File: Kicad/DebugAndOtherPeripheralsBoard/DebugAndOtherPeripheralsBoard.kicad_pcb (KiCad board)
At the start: 2 copper layers, 234.5 x 198.2 mm, 118 parts, among them J1 SCL, SDA, +, GND, J10 USB RWGBS, J11 Standoff Hole, J12 Standoff Hole, J13 Standoff Hole, J14 Standoff Hole, J15 Standoff Hole, J2 Conn_01x08_Pin, J3 Conn_01x01_Pin, J4 Conn_01x01_Pin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

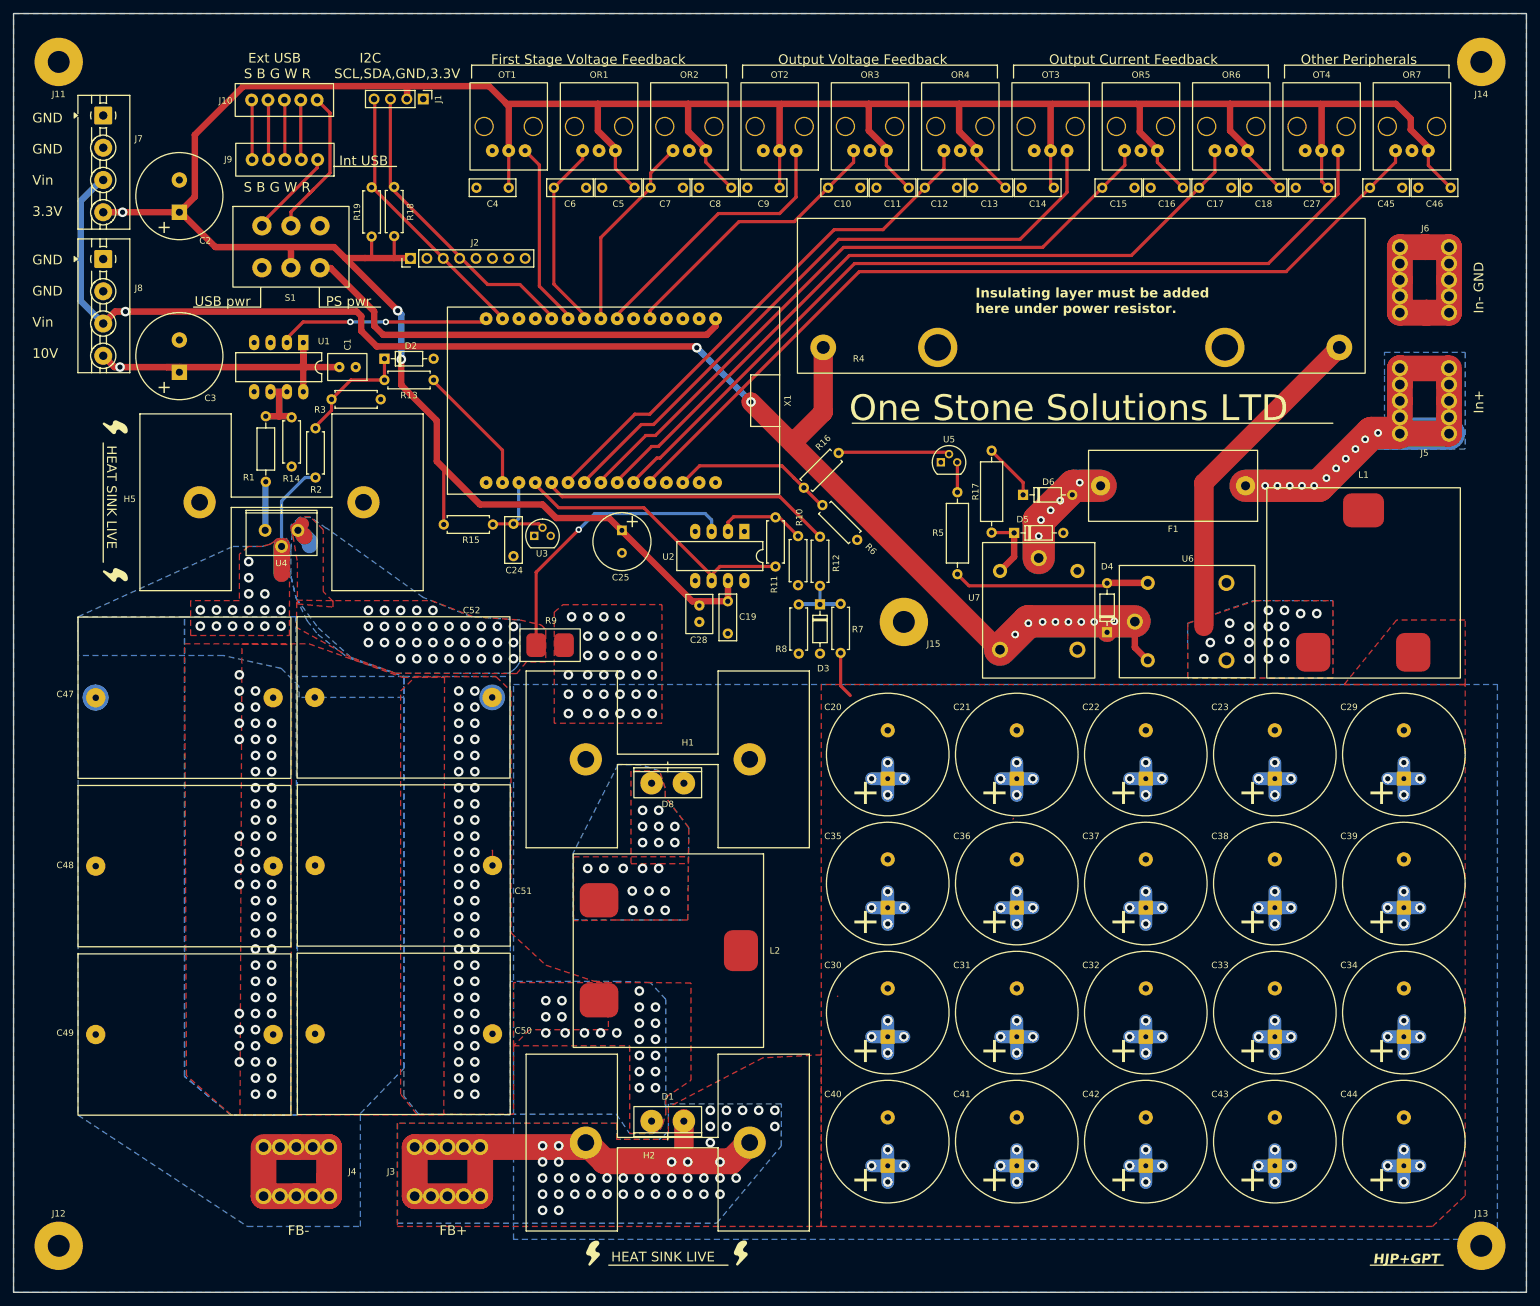
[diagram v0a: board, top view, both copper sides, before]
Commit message: ProgrammingHelper
Utility that has buttons to quickly spin up the console if not open and send commands for configuring building flashing monitoring. This automatically establishes the com port to avoid confusion by myself and potentially flashing the wrong code to the wrong device. Much quicker and cleaner.
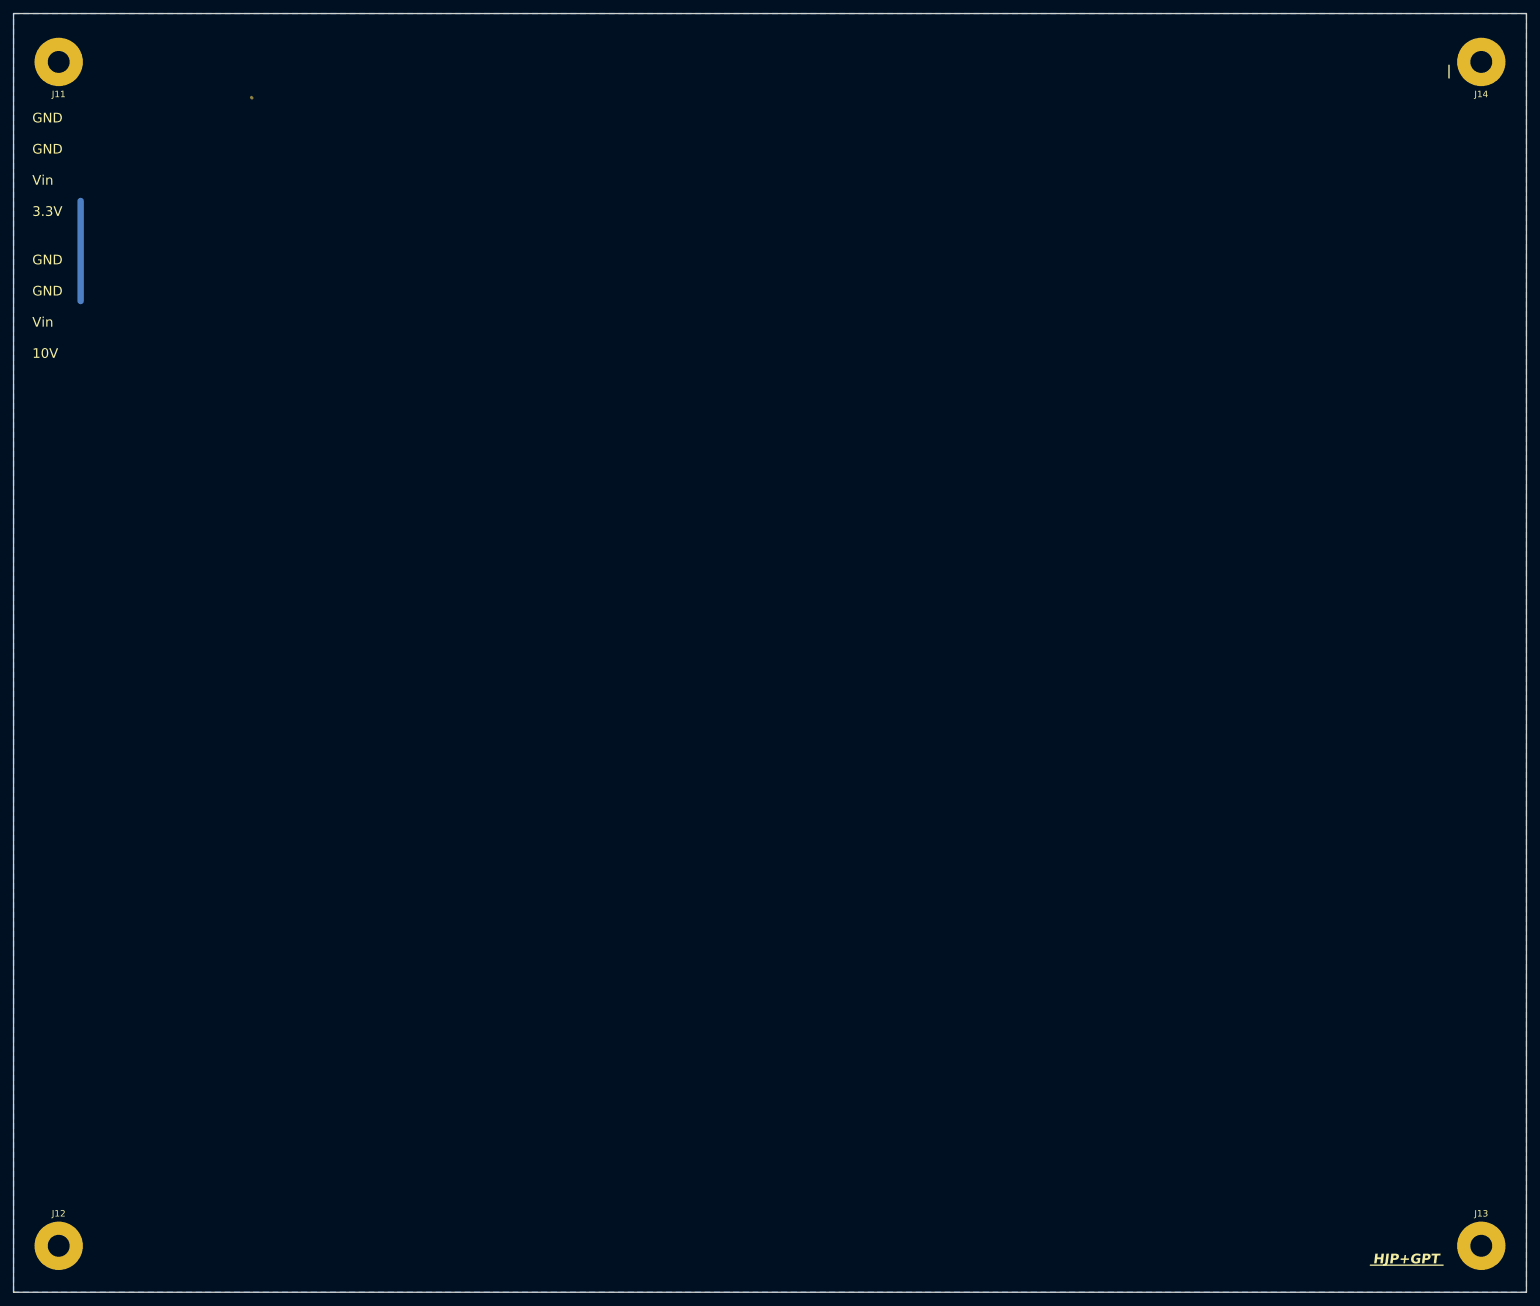
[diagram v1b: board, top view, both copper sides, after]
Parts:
- removed C1: C_drive 1uF, Custom:C320C105K5R5TA
- removed C10, C11, C12, C13, C14, C15, C16, C17, C18, C27, C4, C45, C46, C5, C6, C7, C8, C9: ~, Capacitor_THT:C_Rect_L7.0mm_W2.5mm_P5.00mm
- removed C19: 0.1uF within 2mm, Capacitor_THT:C_Disc_D7.0mm_W2.5mm_P5.00mm
- removed C2, C3: 1000uF UPW1E102MHD, Custom:UPW1E102MHD
- removed C20, C21, C22, C23, C29, C30, C31, C32, C33, C34, C35, C36, C37, C38, C39, C40, C41, C42, C43, C44: EKYB101ELL102MM40S, Custom:EKYB101ELL102MM40S
- removed C24: 0.1uF low ESR Ceramic, Capacitor_THT:C_Rect_L7.0mm_W2.5mm_P5.00mm
- removed C25: 100uF UHD1H101MPD1TD, Custom:UHD1H101MPD1TD
- removed C28: 1uF, Custom:C320C105K5R5TA
- removed C47, C48, C49, C50, C51, C52: R75RR322050L4J, Custom:R75RR322050L4J
- removed D1, D8: MBR40250G, Custom:MBR40250G
- removed D2, D3: ~, Diode_THT:D_DO-35_SOD27_P7.62mm_Horizontal
- removed D4, D5, D6: 1N4148, Diode_THT:D_DO-35_SOD27_P7.62mm_Horizontal
- removed F1: FH-320-NV, Custom:FH-320-NV
- removed H1: Heatsink 1, Custom:647-25ABEP
- removed H2: Heatsink 2, Custom:647-25ABEP
- removed H5: Heatsink 5, Custom:647-25ABEP
- removed J1: SCL, SDA, +, GND, Connector_PinHeader_2.54mm:PinHeader_1x04_P2.54mm_Vertical
- removed J10, J9: USB RWGBS, Custom:USB connection
- removed J15: Standoff Hole, Custom:ContactViaM3
- removed J2: Conn_01x08_Pin, Connector_PinHeader_2.54mm:PinHeader_1x08_P2.54mm_Vertical
- removed J3, J4: Conn_01x01_Pin, Custom:5055556-9
- removed J5: +36V, Custom:5055556-9
- removed J6: GND, Custom:5055556-9
- removed J7, J8: Conn_01x04_Pin, TerminalBlock:TerminalBlock_MaiXu_MX126-5.0-04P_1x04_P5.00mm
- removed L1: SER2918H-223KL, Custom:SER2918H-223KL
- removed L2: 74436411500, Custom:74436411500
- removed OR1, OR2, OR3, OR4, OR5, OR6, OR7: ~, Custom:RS PRO Optical Receiver jack
- removed OT1, OT2, OT3, OT4: ~, Custom:RS Pro Optical Transmitter jack
- removed R1: R_drive 5, Resistor_THT:R_Axial_DIN0207_L6.3mm_D2.5mm_P10.16mm_Horizontal
- removed R10: R_pcfb_in 1K, Resistor_THT:R_Axial_DIN0207_L6.3mm_D2.5mm_P7.62mm_Horizontal
- removed R11: R_pcfb_f 56K, Resistor_THT:R_Axial_DIN0207_L6.3mm_D2.5mm_P7.62mm_Horizontal
- removed R12: R_pfb_i 1K, Resistor_THT:R_Axial_DIN0207_L6.3mm_D2.5mm_P7.62mm_Horizontal
- removed R13: R_sfb_i 1K, Resistor_THT:R_Axial_DIN0207_L6.3mm_D2.5mm_P7.62mm_Horizontal
- removed R14: R_pulldown 1000, Resistor_THT:R_Axial_DIN0207_L6.3mm_D2.5mm_P7.62mm_Horizontal
- removed R15: 3K, Resistor_THT:R_Axial_DIN0207_L6.3mm_D2.5mm_P7.62mm_Horizontal
- removed R16: 1K, Resistor_THT:R_Axial_DIN0207_L6.3mm_D2.5mm_P7.62mm_Horizontal
- removed R17, R5: 1.33K, Resistor_THT:R_Axial_DIN0309_L9.0mm_D3.2mm_P12.70mm_Horizontal
- removed R18, R19: Pullup, Resistor_THT:R_Axial_DIN0207_L6.3mm_D2.5mm_P7.62mm_Horizontal
- removed R2: R_sfb_H 500K, Resistor_THT:R_Axial_DIN0207_L6.3mm_D2.5mm_P7.62mm_Horizontal
- removed R3: R_sfb_L 6.8K, Resistor_THT:R_Axial_DIN0207_L6.3mm_D2.5mm_P7.62mm_Horizontal
- removed R4: ~, Custom:RX24-100W
- removed R6: 10K, Resistor_THT:R_Axial_DIN0207_L6.3mm_D2.5mm_P7.62mm_Horizontal
- removed R7: R_pfb_H 270K, Resistor_THT:R_Axial_DIN0207_L6.3mm_D2.5mm_P7.62mm_Horizontal
- removed R8: R_pfb_ 10K, Resistor_THT:R_Axial_DIN0207_L6.3mm_D2.5mm_P7.62mm_Horizontal
- removed R9: R_pcfb_sense 0.001, Custom:PCS2512FR0010ET
- removed S1: ~, Custom:SLW-1678105-6A-N-D
- removed U1, U2: ~, Package_DIP:CERDIP-8_W7.62mm_SideBrazed_LongPads
- removed U3, U5: ~, Package_TO_SOT_THT:TO-92
- removed U4: ~, Custom:IXFP60N25X3
- removed U6, U7: ~, Custom:AWHSH124D00G
- removed X1: ~, Custom:ESP32_WROOM-32_Dev_Board
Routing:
- net +3V3: track 539.6 -> 0.00 mm, vias 3 -> 0
- net Net-(D1-K): track 296.0 -> 0.00 mm, vias 123 -> 0
- net Net-(D4-K): track 268.3 -> 15.5 mm, vias 11 -> 0
- net Net-(OR7-Vout): track 138.5 -> 0.00 mm
- net Net-(OT4-Vin): track 134.5 -> 0.00 mm
- net Net-(OR6-Vout): track 116.0 -> 0.00 mm
- net Net-(OR5-Vout): track 104.1 -> 0.00 mm
- net Net-(OT3-Vin): track 100.0 -> 0.00 mm
- net Net-(J5-Pin_1): track 96.6 -> 0.00 mm, vias 11 -> 0
- net Net-(OR4-Vout): track 81.4 -> 0.00 mm
- net Net-(X1-3V3): track 69.1 -> 0.00 mm
- net Net-(J4-Pin_1): track 58.6 -> 0.00 mm, vias 16 -> 0
- net Earth: track 56.9 -> 0.00 mm, vias 32 -> 0
- net +10V: track 53.5 -> 0.00 mm, vias 1 -> 0
- net Net-(L1-Pad1): track 51.9 -> 0.00 mm, vias 17 -> 0
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- removed copper zone on F.Cu, net Earth
- removed copper zone on B.Cu, net Net-(D1-A)
- removed copper zone on F.Cu, net Net-(D1-A)
- removed copper zone on B.Cu, net Net-(D1-K)
- removed copper zone on F.Cu, net Net-(D1-K)
- removed copper zone on B.Cu, net Net-(D8-K)
- removed copper zone on F.Cu, net Net-(D8-K)
- removed copper zone on B.Cu, net Net-(J4-Pin_1)
- removed copper zone on F.Cu, net Net-(J4-Pin_1)
- removed copper zone on B.Cu, net Net-(J5-Pin_1)
- removed copper zone on B.Cu, net Net-(L1-Pad1)
- removed copper zone on F.Cu, net Net-(L1-Pad1)
- removed copper zone on B.Cu, net Net-(U2-VIN+)
- removed copper zone on F.Cu, net Net-(U2-VIN+)
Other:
- board text removed: "Ext USB S B G W R"
- board text removed: "FB+"
- board text removed: "FB-"
- board text removed: "First Stage Voltage Feedback"
- board text removed: "HEAT SINK LIVE"
- board text removed: "I2C SCL,SDA,GND,3.3V"
- board text removed: "In+"
- board text removed: "In- GND"
- board text removed: "Insulating layer must be added here under power resistor."
- board text removed: "Int USB"
- board text removed: "One Stone Solutions LTD"
- board text removed: "Other Peripherals"
- board text removed: "Output Current Feedback"
- board text removed: "Output Voltage Feedback"
- board text removed: "PS pwr"
- board text removed: "USB pwr"
